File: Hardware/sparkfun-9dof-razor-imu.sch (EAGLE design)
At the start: 40 parts, among them J1 AVR_SPI_PRG_6PTH, Q1 8MHz, U1 ITG-32001:1, U2 ADXL3451:1, U5 3.3V, U6 ATMEGA328

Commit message: Initial commit of v24.
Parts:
- removed C13, C22, C24, C25, C27, C29: 0.1uF, SparkFun:CAP0603-CAP
- removed C18: 0.22uF, SparkFun:CAP0603-CAP
- removed C21: 4.7uF, SparkFun:CAP0603-CAP
- removed C23, C26: 10uF, SparkFun:CAP_POL1206
- removed JP10: JST_Horizontal, SparkFun:M02PTH
- removed JP11, JP12: FIDUCIAL1X2.5, abes:FIDUCIAL1X2.5
- removed JP2, JP4, JP6: STAND-OFF, SparkFun:STAND-OFF
- removed JP3: LOGO-SFENEW, SparkFun:LOGO-SFENEW
- removed JP7: FTDI Basic, SparkFun:ARDUINO_SERIAL_PROGRAMPTH
- removed LED1: Red, SparkFun:LED0603
- removed Q1: 8MHz, SparkFun:RESONATORSMD
- removed R11: 10K, SparkFun:RESISTOR0603-RES
- removed R12: 330, SparkFun:RESISTOR0603-RES
- removed S2: Power, SparkFun:SWITCH-DPDTSMD
- removed U$1: HMC5883LSMD, SparkFun:HMC5883LSMD
- removed U$4: OSHW-LOGOL, SparkFun:OSHW-LOGOL
- removed U5: 3.3V, SparkFun:V_REG_LDOSMD
- removed U6: ATMEGA328, SparkFun:ATMEGA168
- added C10: 2.2uF, SparkFun-Capacitors:2.2UF-0603-10V-20%
- added C11, C12: 4.7uF, SparkFun-Capacitors:4.7UF0603
- added C4, C6: 0.1uF, SparkFun-Capacitors:0.1UF-0603-25V-(+80/-20%)
- added C5: 0.1uF, SparkFun-Capacitors:0.1UF-0603-100V-10%
- added C7, C8: 15pF, SparkFun-Capacitors:15PF-0603-50V-5%
- added C9: 1.0uF, SparkFun-Capacitors:1.0UF-0603-16V-10%
- added D1: 1A/23V/620mV, SparkFun-DiscreteSemi:DIODE-SCHOTTKY-BAT20J
- added D2: RED, SparkFun-LED:LED-RED0603
- added D4: Yellow, SparkFun-LED:LED-YELLOW0603
- added F1: 6V/0.5A, SparkFun-Fuses:PPTC_HALF-AMP
- added FRAME1: FRAME-LEDGER, SparkFun-Aesthetics:FRAME-LEDGER
- added H1, H2, H3, H4: STAND-OFF, SparkFun-Electromechanical:STAND-OFF
- added J2: (no value), SparkFun-Connectors:CONN_02-JST-2MM-SMT
- added J3: (no value), SparkFun-Connectors:I2C_STANDARD
- added J4: (no value), SparkFun-Connectors:USB_MICROB_PLUGCONN-11752
- added J5, J7: (no value), SparkFun-Connectors:CONN_06NO_SILK_FEMALE_PTH
- added J8: (no value), SparkFun-Connectors:CONN_08"
- added LOGO1: SFE_LOGO_FLAME.1_INCH, SparkFun-Aesthetics:SFE_LOGO_FLAME.1_INCH
- added LOGO2: OSHW-LOGOS, SparkFun-Aesthetics:OSHW-LOGOS
- added LOGO3: SFE_LOGO_NAME.1_INCH, SparkFun-Aesthetics:SFE_LOGO_NAME.1_INCH
- added R3, R5: 1k, SparkFun-Resistors:1KOHM-0603-1/10W-1%
- added R4: 10k, SparkFun-Resistors:10KOHM-0603-1/10W-1%
- added R7, R8: 100k, SparkFun-Resistors:100KOHM-0603-1/10W-1%
- added R9: 2.2k, SparkFun-Resistors:2.2KOHM-0603-1/10W-1%
- added U3: 3.3V, SparkFun-IC-Power:V_REG_AP2112K-3.3V
- added U4: MCP73831, SparkFun-IC-Power:MCP73831
- added Y1: 32.768kHz, SparkFun-Clocks:CRYSTAL-32.768KHZSMD-3.2X1.5
- C1: device SparkFun:CAP0603-CAP -> SparkFun-Capacitors:0.1UF-0603-25V-(+80/-20%)
- C2: value 2.2nF -> 0.1uF; device SparkFun:CAP0603-CAP -> SparkFun-Capacitors:0.1UF-0603-25V-(+80/-20%)
- C3: value 10nF -> 0.1uF; device SparkFun:CAP0603-CAP -> SparkFun-Capacitors:0.1UF-0603-25V-(+80/-20%)
- D3: value Green -> BLUE; device SparkFun:LED0603 -> SparkFun-LED:LED-BLUE0603
- J1: value AVR_SPI_PRG_6PTH -> USD_CONNECTOR; device SparkFun:AVR_SPI_PRG_6PTH -> SparkFun-Connectors:USD_CONNECTOR
- JP1: value JST_Horizontal -> PWR-SELECT; device SparkFun:M02-JST-2MM-SMT -> SparkFun-Jumpers:JUMPER-SMT_3_1-NC_PASTE_NO-SILK
- JP5: value STAND-OFF -> CORTEX_DEBUGPTH; device SparkFun:STAND-OFF -> samd21-temp:CORTEX_DEBUGPTH
- R1: device SparkFun:RESISTOR0603-RES -> SparkFun-Resistors:4.7KOHM-0603-1/10W-1%
- R10: value 10K -> 1k; device SparkFun:RESISTOR0603-RES -> SparkFun-Resistors:1KOHM-0603-1/10W-1%
- R2: value 4.7K -> 4.7k; device SparkFun:RESISTOR0603-RES -> SparkFun-Resistors:4.7KOHM-0603-1/10W-1%
- S1: value Reset -> (none); device SparkFun:SWITCH-MOMENTARY-2SMD -> SparkFun-Electromechanical:SWITCH-SPDT-SMD-A
- U1: value ITG-32001:1 -> ATSAMD21G-A; device Testing:ITG-32001:1 -> SparkFun-IC-Microcontroller:ATSAMD21G-A
- U2: value ADXL3451:1 -> MPU-9250"; device Testing:ADXL3451:1 -> 9dof-devboard-temp:MPU-9250"
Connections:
- removed net DTR: C27.2, JP7.DTR
- removed net MISO: J1.1, U6.PB4(MISO)
- removed net MOSI: J1.4, U6.PB3(MOSI/OC2)
- removed net N$12: D3.A, R12.2
- removed net N$13: Q1.1, U6.PB7(XTAL2/TOSC2)
- removed net N$14: Q1.3, U6.PB6(XTAL1/TOSC1)
- removed net N$15: JP1.2, JP10.2, S2.2, S2.5
- removed net N$38: LED1.A, R11.1
- removed net RAW: C26.+, S2.1, S2.4, U5.EN, U5.IN
- removed net RESET: C27.1, J1.5, R10.1, S1.2, U6.PC6(/RESET)
- removed net RXI: JP7.TXO, U6.PD0(RXD)
- removed net SCK: J1.3, R12.1, U6.PB5(SCK)
- removed net TXO: JP7.RXI, U6.PD1(TXD)
- new net !RESET: JP5.NRESET, R4.1, U1.!RESET!
- new net A0: J8.1, U1.PA02(AIN0/DAC)
- new net A1: J8.2, U1.PB08(AIN2/SER4:0/TC4:0)
- new net A2: U1.PB09(AIN3/SER4:1/TC4:1)
- new net A3: U1.PA04(AIN4/REFB/SER0:0/TC0:0)
- new net A4: U1.PA05(AIN5/SER0:1/TC0:1)
- new net A5: U1.PB02(AIN10/SER5:0)
- new net CHG_LED: R10.1, U4.STAT
- new net D0/RXI: J8.8, U1.PA11(AIN19/SER0:3+)
- new net D1/TXO: J8.7, U1.PA10(AIN18/SER0:2+)
- new net D10: J8.6, U1.PA18(SER1:2+)
- new net D11: J8.5, U1.PA16(I2C/SER1:0+)
- new net D12: J8.4, U1.PA19(SER1:3+)
- new net D13: J8.3, R3.2, U1.PA17(I2C/SER1:1+)
- new net D2/SD_CD: J1.CD1, U1.PA14(XIN/SER2:2+)
- new net D3: U1.PA09(I2C/AIN17/SER0:1+)
- new net D4: U1.PA08(I2C/AIN16/SER0:0+)
- new net D5: U1.PA15(XOUT/SER2:3+)
- new net D6: U1.PA20(SER5:2+)
- new net D7: U1.PA21(SER5:3+)
- new net D8: U1.PA06(AIN6/SER0:2/TC1:0)
- new net D9: U1.PA07(AIN7/SER0:3/TC1:1)
- new net FSYNC: U2.FSYNC
- new net INT: U2.INT
- new net N$10: C11.1, D1.A, J2.1, U4.VBAT
- new net N$11: D4.C, R10.2
- new net N$5: D2.A, R5.1
- new net N$7: R9.2, U4.PROG
- new net N$8: J1.RSV@1, R7.1
- new net N$9: J1.RSV@2, R8.1
- new net REGOUT: C1.1, U2.REGOUT
- new net RX_EDBG: U1.PB23(SER5:3+)
- new net RX_LED: U1.PB03(AIN11/SER5:1)
- new net SD_!CS!: J1.!CS, U1.PA13(I2C/SER2:1+)
- new net SD_MISO: J1.DO, U1.PA12(I2C/SER2:0+)
- new net SD_MOSI: J1.DI, U1.PB10(SER4:2+)
- new net SD_SCK: J1.SCK, U1.PB11(SER4:3+)
- new net SHIELD: J4.SHIELD
- new net SWCLK: JP5.SWDCLK/TCK, U1.PA30(SWCLK/SER1:2+)
- new net SWDIO: JP5.SWDIO/TMS, U1.PA31(SWDIO/SER1:3+)
- new net TX_EDBG: U1.PB22(SER5:2+)
- new net TX_LED: U1.PA27
- new net USB_D+: J4.D+, U1.PA25(SER3:3+)
- new net USB_D-: J4.D-, U1.PA24(SER3:2+)
- new net USB_HOST_EN: U1.PA28
- new net VDDCORE: C4.1, U1.VDDCORE
- new net VIN: C12.1, C9.1, D1.C, D4.A, F1.2, JP1.1, S1.O, U3.IN, U4.VIN
- new net VREG_EN: S1.P, U3.EN
- net 3.3V: now also C10.1, C2.1, C5.1, C6.1, J1.VCC, J3.2, JP1.3, JP5.VCC, R4.2, R5.2, R7.2, R8.2, U1.VDDANA, U1.VDDIN, U1.VDDIO@17, U1.VDDIO@36, U2.!CS, U2.VDDIO, U3.OUT; no longer C13.1, C22.1, C23.+, C24.2, C29.1, J1.2, JP7.VCC, R10.2, R11.2, U$1.S1, U$1.VDD, U$1.VDDIO, U1.VDD, U1.VLOGIC, U2.CS, U2.VSS, U5.OUT, U6.AVCC, U6.VCC@1, U6.VCC@2
- net AREF: now also U1.PA03(AIN1/REFA); no longer C25.2, U6.AREF
- net GND: now also C10.2, C11.2, C12.2, C4.2, C5.2, C6.2, C7.1, C8.2, C9.2, D2.C, J1.GND, J1.SHIELD@1, J1.SHIELD@3, J2.2, J3.1, J4.GND, J7.1, J7.2, J7.3, J7.4, J7.5, J7.6, JP5.GND@3, JP5.GND@5, R9.1, S1.S, U1.GND@18, U1.GND@35, U1.GND@42, U1.GNDANA, U2.AD0/SDO, U2.GND, U3.GND, U4.VSS; no longer C13.2, C21.2, C22.2, C23.-, C24.1, C25.1, C26.-, C29.2, J1.6, JP1.1, JP10.1, JP7.CTS, JP7.GND, LED1.C, Q1.2, S1.1, U$1.GND@1, U$1.GND@2, U1.AD0, U1.CLKIN, U1.GND, U1.RESV-G, U2.GND@2, U2.GND@4, U2.GND@5, U2.SDO, U5.GND, U6.AGND, U6.GND@1, U6.GND@2
- net N$1: now also F1.1, J4.VCC; no longer C18.2, U$1.SETP
- net N$2: now also C7.2, U1.PA00(XIN32/SER1:0/TC2:0), Y1.2; no longer C18.1, U$1.SETC
- net N$3: now also D3.A, R3.1; no longer C1.1, U1.REGOUT
- net N$4: now also C8.1, U1.PA01(XOUT32/SER1:1/TC2:1), Y1.1; no longer C2.1, U1.CPOUT
- net N$6: now also J5.1, J5.2, J5.3, J5.4, J5.5, J5.6, JP1.2; no longer C21.1, U$1.C1
- net SCL: now also J3.4, U1.PA23(I2C/SER3:0+), U2.SCL/SCLK; no longer U$1.SCL, U1.SCL, U2.SCL, U6.PC5(ADC5/SCL)
- net SDA: now also J3.3, U1.PA22(I2C/SER3:0+), U2.SDA/SDI; no longer U$1.SDA, U1.SDA, U2.SDA, U6.PC4(ADC4/SDA)
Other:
- note added: "AD0/SDO defaults to 0V. This sets the I2C address to 0x68. If ADD=VDD, address = 0x69."
- note added: "AP2112K-3.3V ---------------- Iout (max): 600mA Vin (max): 6.5V Vdrop (max): 250mV Iq: 55uA"
- note added: "ATSAMD21G"
- note added: "ATSAMD21G18 VDD Range: 1.62-3.63V"
- note added: "Cortex Debug/Program Connector"
- note added: "LEDs!!!"
- note added: "SJ1 enable's disconnecting the Power LED indicator. For power-saving requirements. Default: closed."
- note added: "USB / Voltage Regulator"
- note added: "VDD 2.4 to 3.6 V"
- note added: "VIN Range: 3.5-6.0V"
- note removed: "0xA6 for write, 0xA7 for read"
- note removed: "0xD0 for write, 0xD1 for read"
- note removed: "ACCEL"
- note removed: "AVR"
- note removed: "AVR SPI"
- note removed: "GYRO"
- note removed: "INTERFACE"
- note removed: "Kade Alexander Jensen"
- note removed: "MAG"
- note removed: "Max Current Output: 150mA"
- note removed: "Max Voltage Input: 16VDC"
- note removed: "POWER"

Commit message: Schematic cleanup, bottom re-routing.
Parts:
- FRAME1: value FRAME-LEDGER -> FRAME-LETTER; device SparkFun-Aesthetics:FRAME-LEDGER -> SparkFun-Aesthetics:FRAME-LETTER
- JP1: value PWR-SELECT -> PW-RAIL
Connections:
- net USB_D+ renamed D+
- net USB_D- renamed D-
- removed net AREF: U1.PA03(AIN1/REFA)
- removed net RX_EDBG: U1.PB23(SER5:3+)
- removed net TX_EDBG: U1.PB22(SER5:2+)
- removed net TX_LED: U1.PA27
- removed net USB_HOST_EN: U1.PA28
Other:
- note added: "ATSAMD21G18"
- note added: "I/O, Power Headers"
- note added: "I2C Header"
- note added: "Jim Lindblom"
- note added: "LiPo Charger"
- note added: "MPU-9250 9DoF"
- note added: "uSD Connector"
- note added: "v24"
- note removed: "ATSAMD21G"
- note removed: "Cortex Debug/Program Connector"
- note removed: "LEDs!!!"
- note removed: "SJ1 enable's disconnecting the Power LED indicator. For power-saving requirements. Default: closed."
- moved on the sheet: C1, C10, C11, C12, C2, C3, C4, C5, C6, C7, C8, C9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

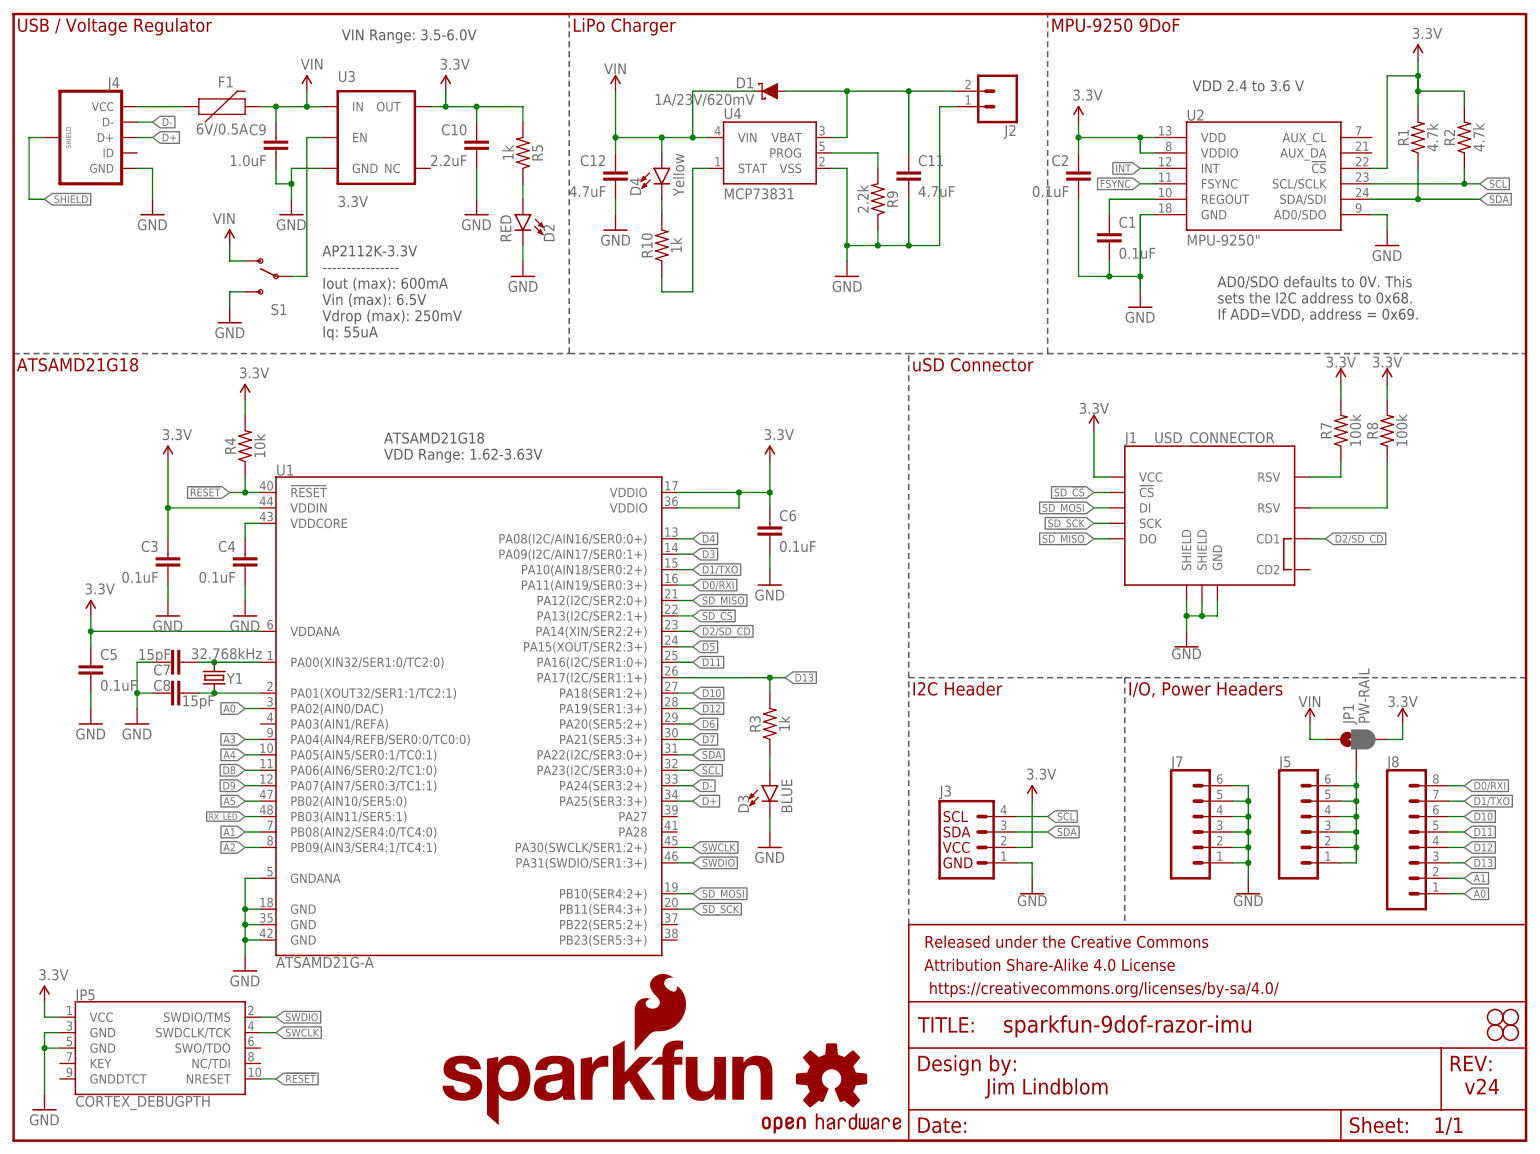
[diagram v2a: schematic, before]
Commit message: Brd/sch tweaks after engineer checklist.
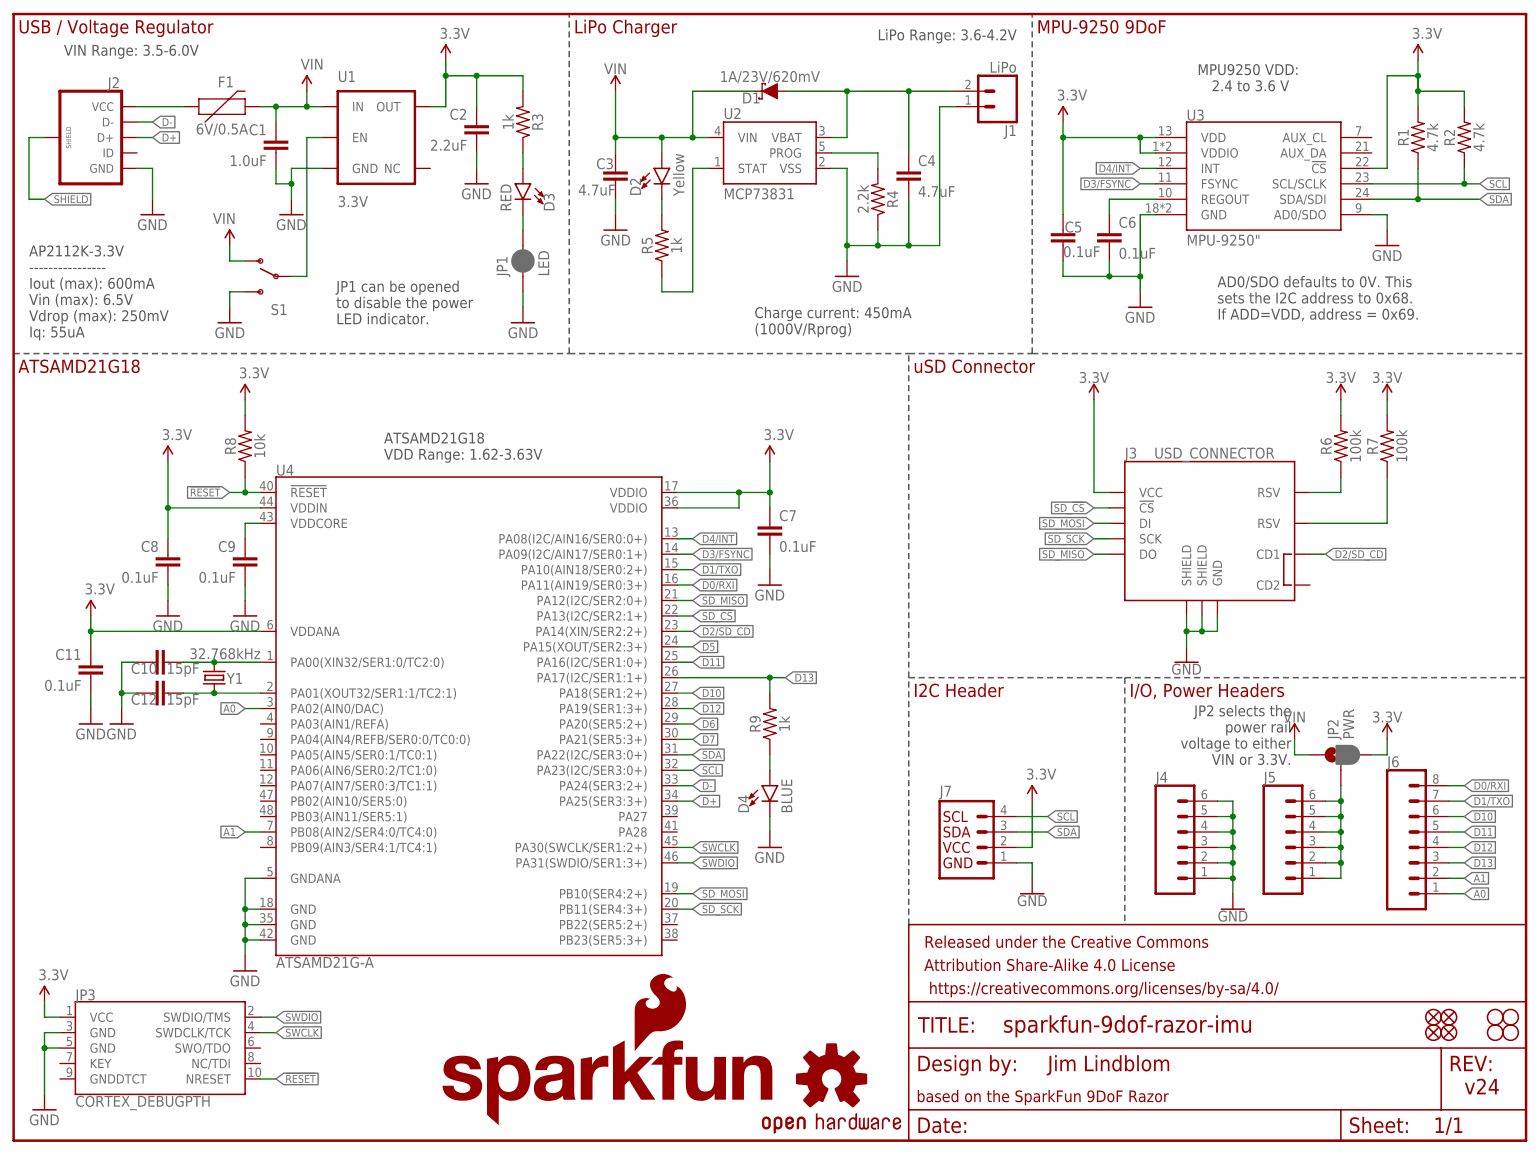
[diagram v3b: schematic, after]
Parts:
- removed R10: 1k, SparkFun-Resistors:1KOHM-0603-1/10W-1%
- added FD1, FD2, FD3, FD4: FIDUCIAL1X2, SparkFun-Aesthetics:FIDUCIAL1X2
- added JP2: PWR, SparkFun-Jumpers:JUMPER-SMT_3_1-NC_PASTE_NO-SILK
- added R6: 100k, SparkFun-Resistors:100KOHM-0603-1/10W-1%
- C1: value 0.1uF -> 1.0uF; device SparkFun-Capacitors:0.1UF-0603-25V-(+80/-20%) -> SparkFun-Capacitors:1.0UF-0603-16V-10%
- C10: value 2.2uF -> 15pF; device SparkFun-Capacitors:2.2UF-0603-10V-20% -> SparkFun-Capacitors:15PF-0603-50V-5%
- C11: value 4.7uF -> 0.1uF; device SparkFun-Capacitors:4.7UF0603 -> SparkFun-Capacitors:0.1UF-0603-100V-10%
- C12: value 4.7uF -> 15pF; device SparkFun-Capacitors:4.7UF0603 -> SparkFun-Capacitors:15PF-0603-50V-5%
- C2: value 0.1uF -> 2.2uF; device SparkFun-Capacitors:0.1UF-0603-25V-(+80/-20%) -> SparkFun-Capacitors:2.2UF-0603-10V-20%
- C3, C4: value 0.1uF -> 4.7uF; device SparkFun-Capacitors:0.1UF-0603-25V-(+80/-20%) -> SparkFun-Capacitors:4.7UF0603
- C5: device SparkFun-Capacitors:0.1UF-0603-100V-10% -> SparkFun-Capacitors:0.1UF-0603-25V-(+80/-20%)
- C7, C8: value 15pF -> 0.1uF; device SparkFun-Capacitors:15PF-0603-50V-5% -> SparkFun-Capacitors:0.1UF-0603-25V-(+80/-20%)
- C9: value 1.0uF -> 0.1uF; device SparkFun-Capacitors:1.0UF-0603-16V-10% -> SparkFun-Capacitors:0.1UF-0603-25V-(+80/-20%)
- D2: value RED -> Yellow; device SparkFun-LED:LED-RED0603 -> SparkFun-LED:LED-YELLOW0603
- D3: value BLUE -> RED; device SparkFun-LED:LED-BLUE0603 -> SparkFun-LED:LED-RED0603
- D4: value Yellow -> BLUE; device SparkFun-LED:LED-YELLOW0603 -> SparkFun-LED:LED-BLUE0603
- J1: value USD_CONNECTOR -> LiPo; device SparkFun-Connectors:USD_CONNECTOR -> SparkFun-Connectors:CONN_02-JST-2MM-SMT
- J2: device SparkFun-Connectors:CONN_02-JST-2MM-SMT -> SparkFun-Connectors:USB_MICROB_PLUGCONN-11752
- J3: value (none) -> USD_CONNECTOR; device SparkFun-Connectors:I2C_STANDARD -> SparkFun-Connectors:USD_CONNECTOR
- J4: device SparkFun-Connectors:USB_MICROB_PLUGCONN-11752 -> SparkFun-Connectors:CONN_06NO_SILK_FEMALE_PTH
- J7: device SparkFun-Connectors:CONN_06NO_SILK_FEMALE_PTH -> SparkFun-Connectors:I2C_STANDARD
- JP1: value PW-RAIL -> LED; device SparkFun-Jumpers:JUMPER-SMT_3_1-NC_PASTE_NO-SILK -> SparkFun-Jumpers:JUMPER-SMT_2_NC_PASTE_NO-SILK
- R4: value 10k -> 2.2k; device SparkFun-Resistors:10KOHM-0603-1/10W-1% -> SparkFun-Resistors:2.2KOHM-0603-1/10W-1%
- R8: value 100k -> 10k; device SparkFun-Resistors:100KOHM-0603-1/10W-1% -> SparkFun-Resistors:10KOHM-0603-1/10W-1%
- R9: value 2.2k -> 1k; device SparkFun-Resistors:2.2KOHM-0603-1/10W-1% -> SparkFun-Resistors:1KOHM-0603-1/10W-1%
- U1: value ATSAMD21G-A -> 3.3V; device SparkFun-IC-Microcontroller:ATSAMD21G-A -> SparkFun-IC-Power:V_REG_AP2112K-3.3V
- U2: value MPU-9250" -> MCP73831; device 9dof-devboard-temp:MPU-9250" -> SparkFun-IC-Power:MCP73831
- U3: value 3.3V -> MPU-9250"; device SparkFun-IC-Power:V_REG_AP2112K-3.3V -> 9dof-devboard-temp:MPU-9250"
- U4: value MCP73831 -> ATSAMD21G-A; device SparkFun-IC-Power:MCP73831 -> SparkFun-IC-Microcontroller:ATSAMD21G-A
- renumbered J8 to J6, JP5 to JP3
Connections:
- removed net A2: U1.PB09(AIN3/SER4:1/TC4:1)
- removed net A3: U1.PA04(AIN4/REFB/SER0:0/TC0:0)
- removed net A4: U1.PA05(AIN5/SER0:1/TC0:1)
- removed net A5: U1.PB02(AIN10/SER5:0)
- removed net D3: U1.PA09(I2C/AIN17/SER0:1+)
- removed net D4: U1.PA08(I2C/AIN16/SER0:0+)
- removed net D8: U1.PA06(AIN6/SER0:2/TC1:0)
- removed net D9: U1.PA07(AIN7/SER0:3/TC1:1)
- removed net FSYNC: U2.FSYNC
- removed net INT: U2.INT
- removed net N$5 (its old number): D2.A, R5.1
- removed net RX_LED: U1.PB03(AIN11/SER5:1)
- new net D3/FSYNC: U3.FSYNC, U4.PA09(I2C/AIN17/SER0:1+)
- new net D4/INT: U3.INT, U4.PA08(I2C/AIN16/SER0:0+)
- new net N$12: D3.C, JP1.2
- new net N$3: D4.A, R9.1
- net !RESET: now also R8.1, U4.!RESET!; no longer R4.1, U1.!RESET!
- net 3.3V: now also C11.1, C7.1, C8.1, J3.VCC, J7.2, JP2.3, R3.2, R6.2, U1.OUT, U3.!CS, U3.VDD, U3.VDDIO, U4.VDDANA, U4.VDDIN, U4.VDDIO@17, U4.VDDIO@36; no longer C10.1, C3.1, C6.1, J1.VCC, J3.2, JP1.3, R4.2, R5.2, U1.VDDANA, U1.VDDIN, U1.VDDIO@17, U1.VDDIO@36, U2.!CS, U2.VDD, U2.VDDIO, U3.OUT
- net A0: now also U4.PA02(AIN0/DAC); no longer U1.PA02(AIN0/DAC)
- net A1: now also U4.PB08(AIN2/SER4:0/TC4:0); no longer U1.PB08(AIN2/SER4:0/TC4:0)
- net CHG_LED: now also R5.1, U2.STAT; no longer R10.1, U4.STAT
- net D+: now also J2.D+, U4.PA25(SER3:3+); no longer J4.D+, U1.PA25(SER3:3+)
- net D-: now also J2.D-, U4.PA24(SER3:2+); no longer J4.D-, U1.PA24(SER3:2+)
- net D0/RXI: now also U4.PA11(AIN19/SER0:3+); no longer U1.PA11(AIN19/SER0:3+)
- net D1/TXO: now also U4.PA10(AIN18/SER0:2+); no longer U1.PA10(AIN18/SER0:2+)
- net D10: now also U4.PA18(SER1:2+); no longer U1.PA18(SER1:2+)
- net D11: now also U4.PA16(I2C/SER1:0+); no longer U1.PA16(I2C/SER1:0+)
- net D12: now also U4.PA19(SER1:3+); no longer U1.PA19(SER1:3+)
- net D13: now also R9.2, U4.PA17(I2C/SER1:1+); no longer R3.2, U1.PA17(I2C/SER1:1+)
- net D2/SD_CD: now also J3.CD1, U4.PA14(XIN/SER2:2+); no longer J1.CD1, U1.PA14(XIN/SER2:2+)
- net D5: now also U4.PA15(XOUT/SER2:3+); no longer U1.PA15(XOUT/SER2:3+)
- net D6: now also U4.PA20(SER5:2+); no longer U1.PA20(SER5:2+)
- net D7: now also U4.PA21(SER5:3+); no longer U1.PA21(SER5:3+)
- net GND: now also C10.1, C7.2, D4.C, J1.2, J2.GND, J3.GND, J3.SHIELD@1, J3.SHIELD@3, J4.1, J4.2, J4.3, J4.4, J4.5, J4.6, JP1.1, R4.1, U1.GND, U2.VSS, U3.AD0/SDO, U4.GND@18, U4.GND@35, U4.GND@42, U4.GNDANA; no longer C10.2, C7.1, D2.C, D3.C, J1.GND, J1.SHIELD@1, J1.SHIELD@3, J2.2, J3.1, J4.GND, J7.2, J7.3, J7.4, J7.5, J7.6, R9.1, U1.GND@18, U1.GND@35, U1.GND@42, U1.GNDANA, U2.AD0/SDO, U2.GND, U4.VSS
- net N$1: now also J2.VCC; no longer J4.VCC
- net N$10: now also C4.1, J1.1, U2.VBAT; no longer C11.1, J2.1, U4.VBAT
- net N$11: now also D2.C, R5.2; no longer D4.C, R10.2
- net N$2: now also C10.2, U4.PA00(XIN32/SER1:0/TC2:0); no longer C7.2, U1.PA00(XIN32/SER1:0/TC2:0)
- net N$4: now also C12.1, U4.PA01(XOUT32/SER1:1/TC2:1); no longer C8.1, U1.PA01(XOUT32/SER1:1/TC2:1)
- net N$6: now also JP2.2; no longer JP1.2
- net N$7: now also R4.2, U2.PROG; no longer R9.2, U4.PROG
- net N$8: now also J3.RSV@1, R6.1; no longer J1.RSV@1, R7.1
- net N$9: now also J3.RSV@2, R7.1; no longer J1.RSV@2, R8.1
- net REGOUT: now also C6.1, U3.REGOUT; no longer C1.1, U2.REGOUT
- net SCL: now also J7.4, U3.SCL/SCLK, U4.PA23(I2C/SER3:0+); no longer J3.4, U1.PA23(I2C/SER3:0+), U2.SCL/SCLK
- net SDA: now also J7.3, U3.SDA/SDI, U4.PA22(I2C/SER3:0+); no longer J3.3, U1.PA22(I2C/SER3:0+), U2.SDA/SDI
- net SD_!CS!: now also J3.!CS, U4.PA13(I2C/SER2:1+); no longer J1.!CS, U1.PA13(I2C/SER2:1+)
- net SD_MISO: now also J3.DO, U4.PA12(I2C/SER2:0+); no longer J1.DO, U1.PA12(I2C/SER2:0+)
- net SD_MOSI: now also J3.DI, U4.PB10(SER4:2+); no longer J1.DI, U1.PB10(SER4:2+)
- net SD_SCK: now also J3.SCK, U4.PB11(SER4:3+); no longer J1.SCK, U1.PB11(SER4:3+)
- net SHIELD: now also J2.SHIELD; no longer J4.SHIELD
- net SWCLK: now also U4.PA30(SWCLK/SER1:2+); no longer U1.PA30(SWCLK/SER1:2+)
- net SWDIO: now also U4.PA31(SWDIO/SER1:3+); no longer U1.PA31(SWDIO/SER1:3+)
- net VDDCORE: now also C9.1, U4.VDDCORE; no longer C4.1, U1.VDDCORE
- net VIN: now also C1.1, C3.1, D2.A, JP2.1, U1.IN, U2.VIN; no longer C12.1, C9.1, D4.A, JP1.1, U3.IN, U4.VIN
- net VREG_EN: now also U1.EN; no longer U3.EN
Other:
- note added: "Charge current: 450mA (1000V/Rprog)"
- note added: "JP1 can be opened to disable the power LED indicator."
- note added: "JP2 selects the power rail voltage to either VIN or 3.3V."
- note added: "LiPo Range: 3.6-4.2V"
- note added: "MPU9250 VDD: 2.4 to 3.6 V"
- note added: "based on the SparkFun 9DoF Razor"
- note removed: "VDD 2.4 to 3.6 V"
- moved on the sheet: C1, C10, C11, C12, C2, C3, C4, C5, C6, C7, C8, C9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
